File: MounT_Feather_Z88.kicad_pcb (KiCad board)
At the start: 2 copper layers, 50.8 x 22.9 mm, 10 parts, among them J1 Adafruit_Feather, J2 DE9_Male, U1 MAX3232

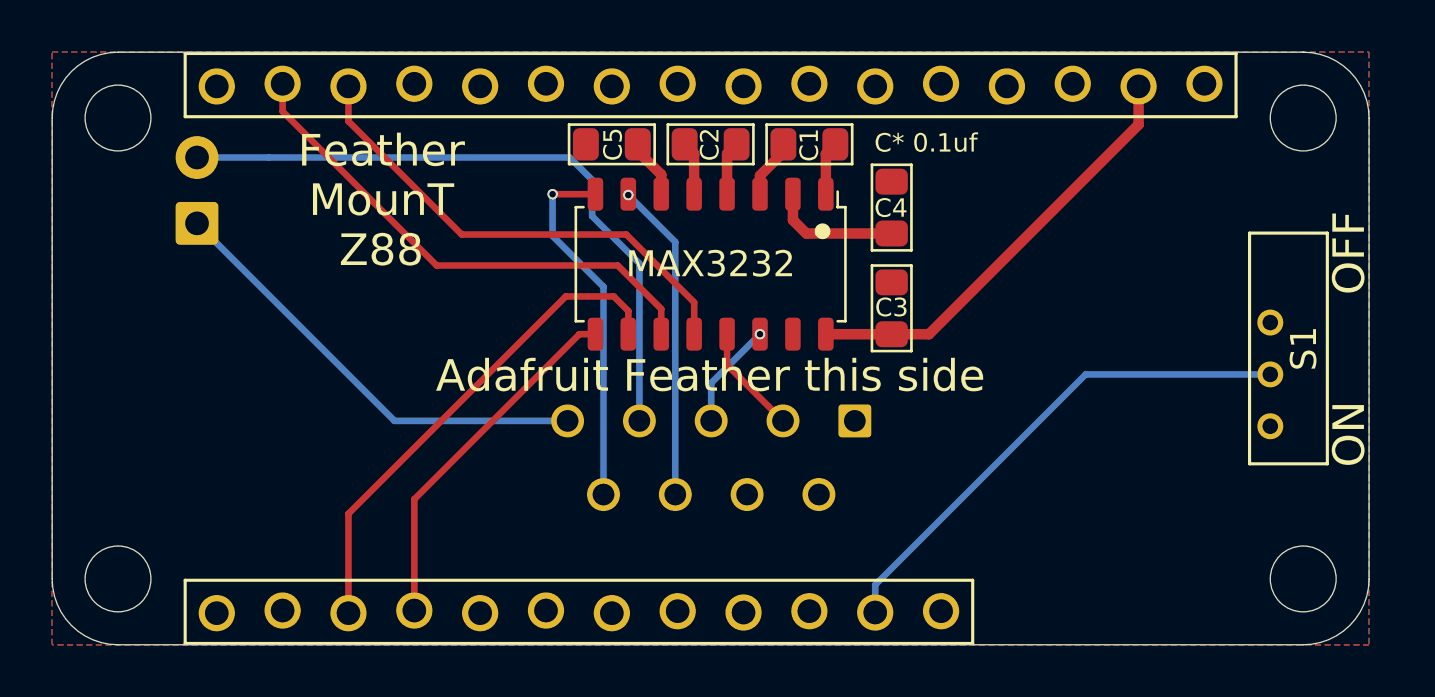
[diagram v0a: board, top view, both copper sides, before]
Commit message: WP2 & Z88, move DE9 shell away from pins. Increase solder pads in S1.
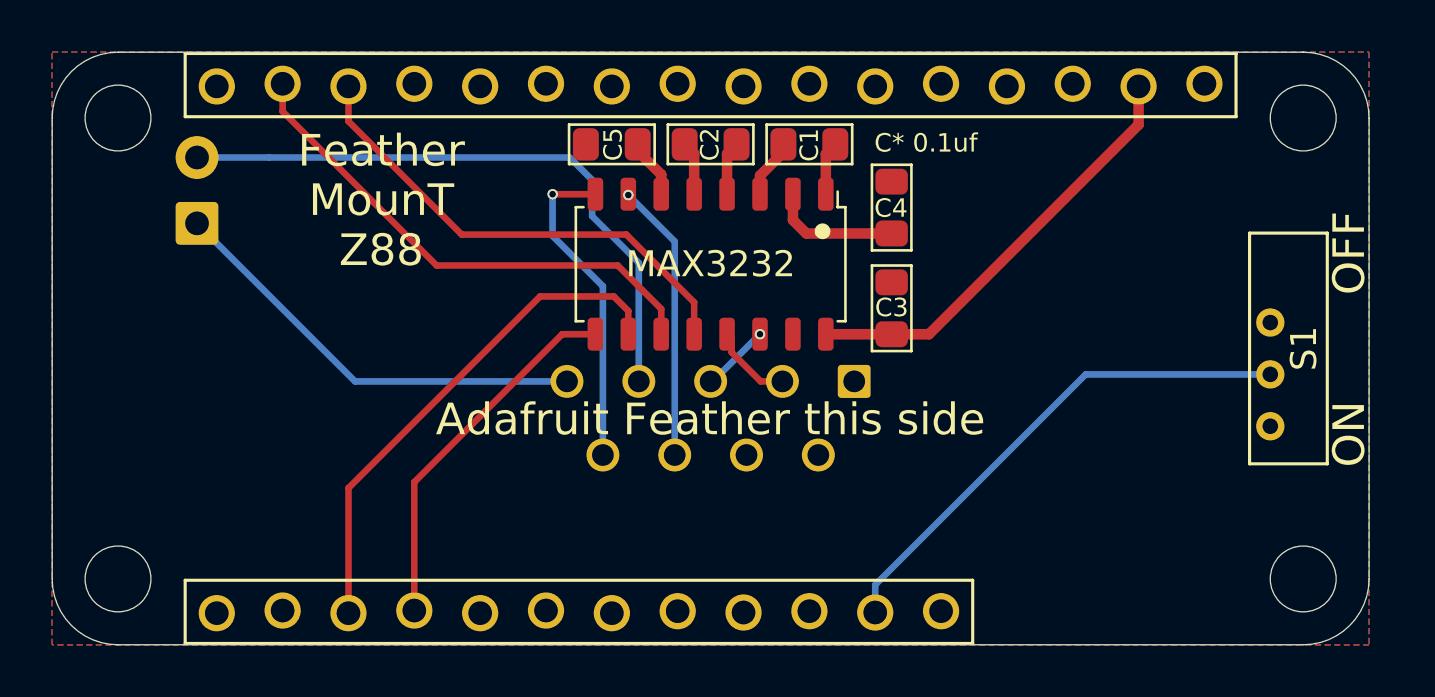
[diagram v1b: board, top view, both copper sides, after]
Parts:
- moved J2 1.52 mm to (152.9, 97.8)
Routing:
- net /DCD_232: track 12.3 -> 10.8 mm
- net /DTR_232: track 14.0 -> 12.5 mm
- net /RTS_232: track 25.6 -> 24.1 mm
- net /RX_232: track 4.12 -> 2.64 mm
- net /TX_232: track 4.24 -> 3.20 mm
- net /CTS_232: track 17.5 -> 16.8 mm
- net /DTR_TTL: track 19.3 -> 19.9 mm

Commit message: use 6mil stagger, 4mil wasn't good enough
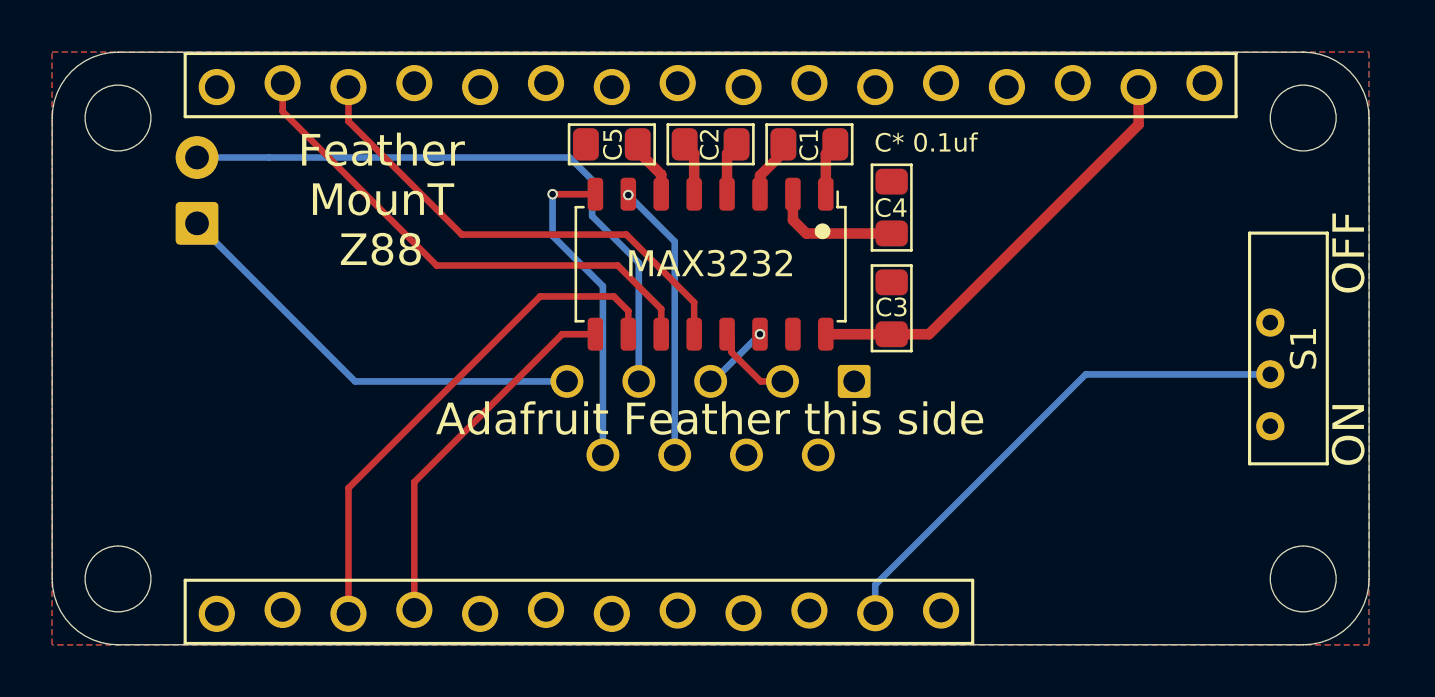
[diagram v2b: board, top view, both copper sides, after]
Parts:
- J1: footprint 0_LOCAL:Adafruit_Feather_stagger_4mil -> 0_LOCAL:Adafruit_Feather_stagger_6mil
